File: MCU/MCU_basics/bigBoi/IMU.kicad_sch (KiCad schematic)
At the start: 10 parts, among them U1 BNO086, Y1 32k

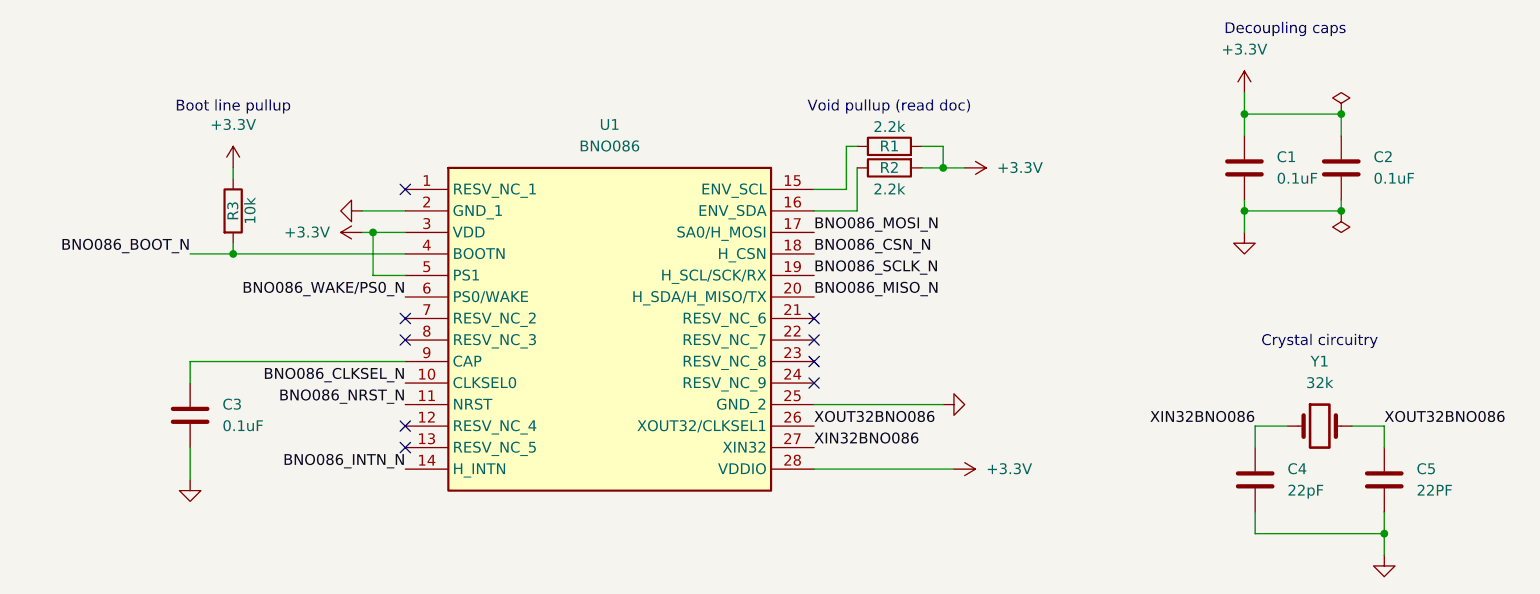
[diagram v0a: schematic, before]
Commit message: schematic connections
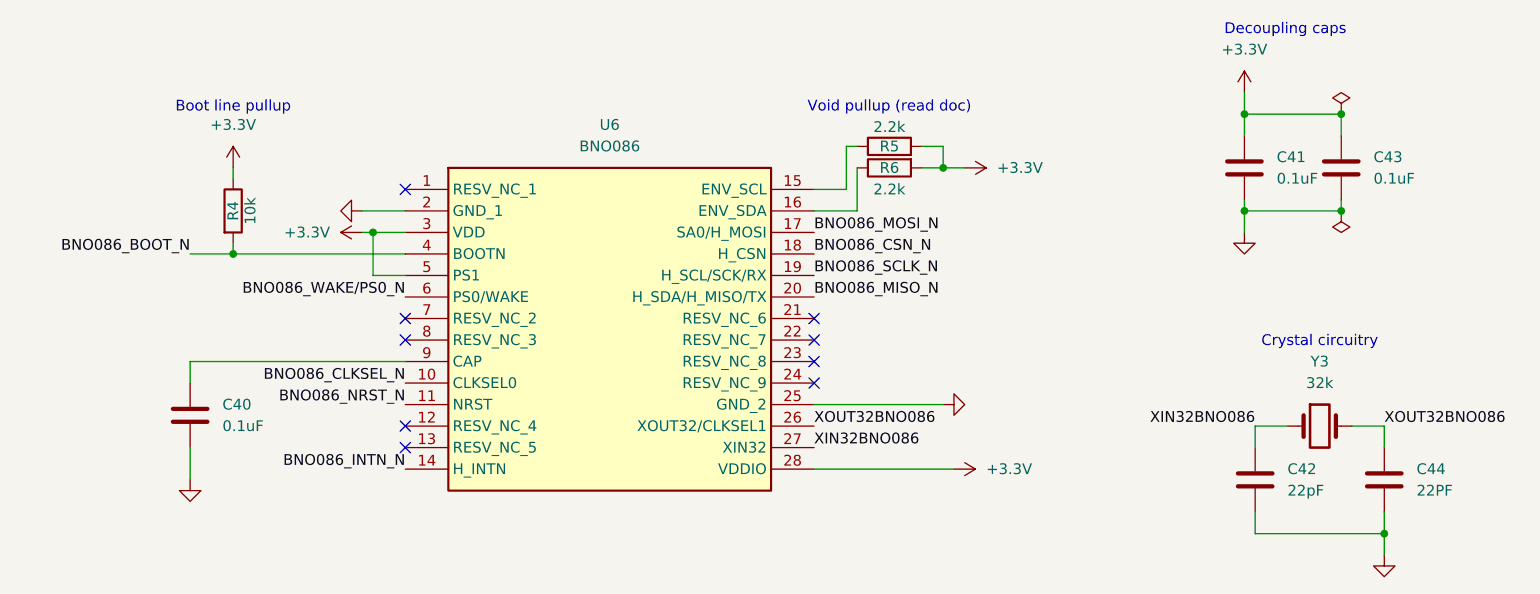
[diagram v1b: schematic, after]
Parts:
- renumbered C3 to C40, C1 to C41, C4 to C42, C2 to C43, C5 to C44, R3 to R4, R1 to R5, R2 to R6, U1 to U6, Y1 to Y3
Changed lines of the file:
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@@
 		(dnp no)
 		(fields_autoplaced yes)
-		(property "Reference" "#PWR046"
+		(property "Reference" "#PWR063"
 			(at 176.53 66.04 0)
 			(hide yes)
@@
 			(project "bigBoi"
 				(path "/0a118c22-2522-42a6-b7a6-70c79326ece4/c267ab07-0814-4d37-8bca-35bdb5036057"
-					(reference "#PWR046")
+					(reference "#PWR063")
 					(unit 1)
 				)
@@
 		(dnp no)
 		(fields_autoplaced yes)
-		(property "Reference" "#PWR040"
+		(property "Reference" "#PWR057"
 			(at 88.9 109.22 0)
 			(hide yes)
@@
 			(project "bigBoi"
 				(path "/0a118c22-2522-42a6-b7a6-70c79326ece4/c267ab07-0814-4d37-8bca-35bdb5036057"
-					(reference "#PWR040")
+					(reference "#PWR057")
 					(unit 1)
 				)
@@
 		(dnp no)
 		(fields_autoplaced yes)
-		(property "Reference" "Y1"
+		(property "Reference" "Y3"
 			(at 222.25 88.9 0)
 			(show_name no)
@@
 			(project "bigBoi"
 				(path "/0a118c22-2522-42a6-b7a6-70c79326ece4/c267ab07-0814-4d37-8bca-35bdb5036057"
-					(reference "Y1")
+					(reference "Y3")
 					(unit 1)
 				)
@@
 		(dnp no)
 		(fields_autoplaced yes)
-		(property "Reference" "C2"
+		(property "Reference" "C43"
 			(at 228.6 64.7699 0)
 			(show_name no)
@@
 			(project "bigBoi"
 				(path "/0a118c22-2522-42a6-b7a6-70c79326ece4/c267ab07-0814-4d37-8bca-35bdb5036057"
-					(reference "C2")
+					(reference "C43")
 					(unit 1)
 				)
@@
 		(in_pos_files yes)
 		(dnp no)
-		(property "Reference" "R2"
+		(property "Reference" "R6"
 			(at 171.45 66.04 90)
 			(show_name no)
@@
 			(project "bigBoi"
 				(path "/0a118c22-2522-42a6-b7a6-70c79326ece4/c267ab07-0814-4d37-8bca-35bdb5036057"
-					(reference "R2")
+					(reference "R6")
 					(unit 1)
 				)
@@
 		(dnp no)
 		(fields_autoplaced yes)
-		(property "Reference" "#PWR047"
+		(property "Reference" "#PWR064"
 			(at 213.36 60.96 0)
 			(hide yes)
@@
 			(project "bigBoi"
 				(path "/0a118c22-2522-42a6-b7a6-70c79326ece4/c267ab07-0814-4d37-8bca-35bdb5036057"
-					(reference "#PWR047")
+					(reference "#PWR064")
 					(unit 1)
 				)
@@
 		(dnp no)
 		(fields_autoplaced yes)
-		(property "Reference" "#PWR049"
+		(property "Reference" "#PWR066"
 			(at 229.87 118.11 0)
 			(hide yes)
@@
 			(project "bigBoi"
 				(path "/0a118c22-2522-42a6-b7a6-70c79326ece4/c267ab07-0814-4d37-8bca-35bdb5036057"
-					(reference "#PWR049")
+					(reference "#PWR066")
 					(unit 1)
 				)
@@
 		(dnp no)
 		(fields_autoplaced yes)
-		(property "Reference" "C3"
+		(property "Reference" "C40"
 			(at 92.71 93.9799 0)
 			(show_name no)
@@
 			(project "bigBoi"
 				(path "/0a118c22-2522-42a6-b7a6-70c79326ece4/c267ab07-0814-4d37-8bca-35bdb5036057"
-					(reference "C3")
+					(reference "C40")
 					(unit 1)
 				)
@@
 		(dnp no)
 		(fields_autoplaced yes)
-		(property "Reference" "U1"
+		(property "Reference" "U6"
 			(at 138.43 60.96 0)
 			(show_name no)
@@
 			(project "bigBoi"
 				(path "/0a118c22-2522-42a6-b7a6-70c79326ece4/c267ab07-0814-4d37-8bca-35bdb5036057"
-					(reference "U1")
+					(reference "U6")
 					(unit 1)
 				)
@@
 		(dnp no)
 		(fields_autoplaced yes)
-		(property "Reference" "#FLG02"
+		(property "Reference" "#FLG03"
 			(at 224.79 57.785 0)
 			(hide yes)
@@
 			(project "bigBoi"
 				(path "/0a118c22-2522-42a6-b7a6-70c79326ece4/c267ab07-0814-4d37-8bca-35bdb5036057"
-					(reference "#FLG02")
+					(reference "#FLG03")
 					(unit 1)
 				)
@@
 		(dnp no)
 		(fields_autoplaced yes)
-		(property "Reference" "C5"
+		(property "Reference" "C44"
 			(at 233.68 101.5999 0)
 			(show_name no)
@@
 			(project "bigBoi"
 				(path "/0a118c22-2522-42a6-b7a6-70c79326ece4/c267ab07-0814-4d37-8bca-35bdb5036057"
-					(reference "C5")
+					(reference "C44")
 					(unit 1)
 				)
@@
 		(dnp no)
 		(fields_autoplaced yes)
-		(property "Reference" "#PWR045"
+		(property "Reference" "#PWR062"
 			(at 175.26 101.6 0)
 			(hide yes)
@@
 			(project "bigBoi"
 				(path "/0a118c22-2522-42a6-b7a6-70c79326ece4/c267ab07-0814-4d37-8bca-35bdb5036057"
-					(reference "#PWR045")
+					(reference "#PWR062")
 					(unit 1)
 				)
@@
 		(dnp no)
 		(fields_autoplaced yes)
-		(property "Reference" "C1"
+		(property "Reference" "C41"
 			(at 217.17 64.7699 0)
 			(show_name no)
@@
 			(project "bigBoi"
 				(path "/0a118c22-2522-42a6-b7a6-70c79326ece4/c267ab07-0814-4d37-8bca-35bdb5036057"
-					(reference "C1")
+					(reference "C41")
 					(unit 1)
 				)
@@
 		(in_pos_files yes)
 		(dnp no)
-		(property "Reference" "R3"
+		(property "Reference" "R4"
 			(at 93.98 71.12 90)
 			(show_name no)
@@
 			(project "bigBoi"
 				(path "/0a118c22-2522-42a6-b7a6-70c79326ece4/c267ab07-0814-4d37-8bca-35bdb5036057"
-					(reference "R3")
+					(reference "R4")
 					(unit 1)
 				)
@@
 		(dnp no)
 		(fields_autoplaced yes)
-		(property "Reference" "#FLG02"
+		(property "Reference" "#FLG04"
 			(at 224.79 73.025 0)
 			(hide yes)
@@
 			(project "bigBoi"
 				(path "/0a118c22-2522-42a6-b7a6-70c79326ece4/c267ab07-0814-4d37-8bca-35bdb5036057"
-					(reference "#FLG02")
+					(reference "#FLG04")
 					(unit 1)
 				)
@@
 		(dnp no)
 		(fields_autoplaced yes)
-		(property "Reference" "#PWR043"
+		(property "Reference" "#PWR060"
 			(at 113.03 73.66 0)
 			(hide yes)
@@
 			(project "bigBoi"
 				(path "/0a118c22-2522-42a6-b7a6-70c79326ece4/c267ab07-0814-4d37-8bca-35bdb5036057"
-					(reference "#PWR043")
+					(reference "#PWR060")
 					(unit 1)
 				)
@@
 		(dnp no)
 		(fields_autoplaced yes)
-		(property "Reference" "#PWR041"
+		(property "Reference" "#PWR058"
 			(at 93.98 69.85 0)
 			(hide yes)
@@
 			(project "bigBoi"
 				(path "/0a118c22-2522-42a6-b7a6-70c79326ece4/c267ab07-0814-4d37-8bca-35bdb5036057"
-					(reference "#PWR041")
+					(reference "#PWR058")
 					(unit 1)
 				)
@@
 		(dnp no)
 		(fields_autoplaced yes)
-		(property "Reference" "C4"
+		(property "Reference" "C42"
 			(at 218.44 101.5999 0)
 			(show_name no)
@@
 			(project "bigBoi"
 				(path "/0a118c22-2522-42a6-b7a6-70c79326ece4/c267ab07-0814-4d37-8bca-35bdb5036057"
-					(reference "C4")
+					(reference "C42")
 					(unit 1)
 				)
@@
 		(dnp no)
 		(fields_autoplaced yes)
-		(property "Reference" "#PWR044"
+		(property "Reference" "#PWR061"
 			(at 184.15 93.98 0)
 			(hide yes)
@@
 			(project "bigBoi"
 				(path "/0a118c22-2522-42a6-b7a6-70c79326ece4/c267ab07-0814-4d37-8bca-35bdb5036057"
-					(reference "#PWR044")
+					(reference "#PWR061")
 					(unit 1)
 				)
@@
 		(dnp no)
 		(fields_autoplaced yes)
-		(property "Reference" "#PWR042"
+		(property "Reference" "#PWR059"
 			(at 102.87 71.12 0)
 			(hide yes)
@@
 			(project "bigBoi"
 				(path "/0a118c22-2522-42a6-b7a6-70c79326ece4/c267ab07-0814-4d37-8bca-35bdb5036057"
-					(reference "#PWR042")
+					(reference "#PWR059")
 					(unit 1)
 				)
@@
 		(dnp no)
 		(fields_autoplaced yes)
-		(property "Reference" "#PWR048"
+		(property "Reference" "#PWR065"
 			(at 213.36 80.01 0)
 			(hide yes)
@@
 			(project "bigBoi"
 				(path "/0a118c22-2522-42a6-b7a6-70c79326ece4/c267ab07-0814-4d37-8bca-35bdb5036057"
-					(reference "#PWR048")
+					(reference "#PWR065")
 					(unit 1)
 				)
@@
 		(in_pos_files yes)
 		(dnp no)
-		(property "Reference" "R1"
+		(property "Reference" "R5"
 			(at 171.45 63.5 90)
 			(show_name no)
@@
 			(project "bigBoi"
 				(path "/0a118c22-2522-42a6-b7a6-70c79326ece4/c267ab07-0814-4d37-8bca-35bdb5036057"
-					(reference "R1")
-					(unit 1)
-				)
+					(reference "R5")
+					(unit 1)
+				)

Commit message: ERC resolving
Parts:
- C40, C41, C42, C43, C44: footprint (none) -> Capacitor_SMD:C_0402_1005Metric
- R4, R5, R6: footprint (none) -> Resistor_SMD:R_0402_1005Metric
- U6: footprint BNO086 -> Nebula-footprints:BNO086
- Y3: value 32k -> 32kHz; footprint (none) -> Crystal:Crystal_SMD_3215-2Pin_3.2x1.5mm

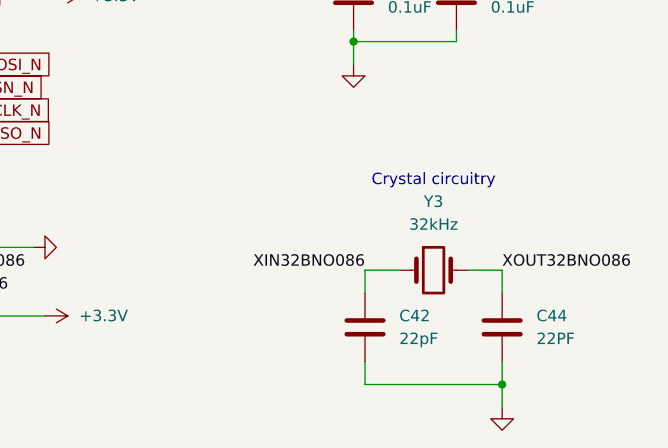
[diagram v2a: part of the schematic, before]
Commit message: Store deler av VBUS og USB
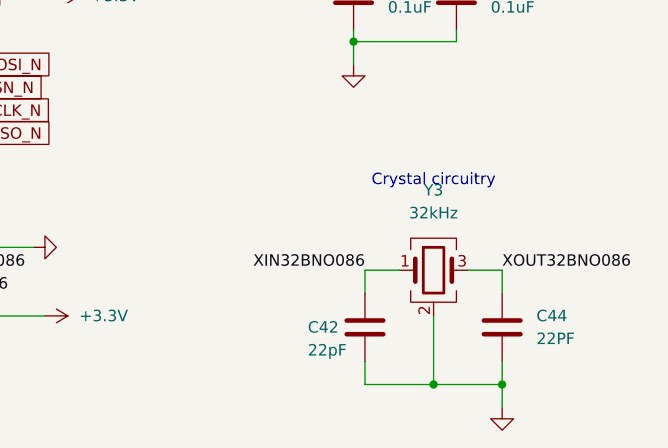
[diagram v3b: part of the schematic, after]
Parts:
- removed Y3: 32kHz, Crystal:Crystal_SMD_3215-2Pin_3.2x1.5mm, symbol Device:Crystal
- added Y3: 32kHz, Crystal:Crystal_SMD_3225-4Pin_3.2x2.5mm_HandSoldering, symbol Device:Crystal_GND24
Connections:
- net GND: now also Y3.2 (G), Y3.4 (G)
- net XIN32BNO086: now also Y3.1
- net XOUT32BNO086: now also Y3.3
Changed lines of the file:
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@@
+	)
+	(junction
+		(at 222.25 109.22)
+		(diameter 0)
+		(color 0 0 0 0)
 	)
 	(junction
@@
 	(wire
 		(pts
+			(xy 222.25 101.6) (xy 222.25 109.22)
+		)
+		(stroke
+			(width 0)
+			(type default)
+		)
+	)
+	(wire
+		(pts
 			(xy 224.79 71.12) (xy 213.36 71.12)
 		)
@@
 	(wire
 		(pts
+			(xy 222.25 109.22) (xy 229.87 109.22)
+		)
+		(stroke
+			(width 0)
+			(type default)
+		)
+	)
+	(wire
+		(pts
 			(xy 166.37 63.5) (xy 166.37 68.58)
 		)
@@
 	(wire
 		(pts
-			(xy 214.63 109.22) (xy 229.87 109.22)
+			(xy 214.63 109.22) (xy 222.25 109.22)
 		)
 		(stroke
@@
 				(path "/0a118c22-2522-42a6-b7a6-70c79326ece4/c267ab07-0814-4d37-8bca-35bdb5036057"
 					(reference "#PWR057")
-					(unit 1)
-				)
-			)
-		)
-	)
-	(symbol
-		(lib_id "Device:Crystal")
-		(at 222.25 96.52 0)
-		(unit 1)
-		(body_style 1)
-		(exclude_from_sim no)
-		(in_bom yes)
-		(on_board yes)
-		(in_pos_files yes)
-		(dnp no)
-		(fields_autoplaced yes)
-		(property "Reference" "Y3"
-			(at 222.25 88.9 0)
-			(show_name no)
-			(do_not_autoplace no)
-			(effects
-				(font
-					(size 1.27 1.27)
-				)
-			)
-		)
-		(property "Value" "32kHz"
-			(at 222.25 91.44 0)
-			(show_name no)
-			(do_not_autoplace no)
-			(effects
-				(font
-					(size 1.27 1.27)
-				)
-			)
-		)
-		(property "Footprint" "Crystal:Crystal_SMD_3215-2Pin_3.2x1.5mm"
-			(at 222.25 96.52 0)
-			(hide yes)
-			(show_name no)
-			(do_not_autoplace no)
-			(effects
-				(font
-					(size 1.27 1.27)
-				)
-			)
-		)
-		(property "Datasheet" ""
-			(at 222.25 96.52 0)
-			(hide yes)
-			(show_name no)
-			(do_not_autoplace no)
-			(effects
-				(font
-					(size 1.27 1.27)
-				)
-			)
-		)
-		(property "Description" "Two pin crystal"
-			(at 222.25 96.52 0)
-			(hide yes)
-			(show_name no)
-			(do_not_autoplace no)
-			(effects
-				(font
-					(size 1.27 1.27)
-				)
-			)
-		)
-		(pin "1"
-		)
-		(pin "2"
-		)
-		(instances
-			(project "bigBoi"
-				(path "/0a118c22-2522-42a6-b7a6-70c79326ece4/c267ab07-0814-4d37-8bca-35bdb5036057"
-					(reference "Y3")
 					(unit 1)
 				)
@@
 	)
 	(symbol
+		(lib_id "Device:Crystal_GND24")
+		(at 222.25 96.52 0)
+		(unit 1)
+		(body_style 1)
+		(exclude_from_sim no)
+		(in_bom yes)
+		(on_board yes)
+		(in_pos_files yes)
+		(dnp no)
+		(fields_autoplaced yes)
+		(property "Reference" "Y3"
+			(at 222.25 87.63 0)
+			(show_name no)
+			(do_not_autoplace no)
+			(effects
+				(font
+					(size 1.27 1.27)
+				)
+			)
+		)
+		(property "Value" "32kHz"
+			(at 222.25 90.17 0)
+			(show_name no)
+			(do_not_autoplace no)
+			(effects
+				(font
+					(size 1.27 1.27)
+				)
+			)
+		)
+		(property "Footprint" "Crystal:Crystal_SMD_3225-4Pin_3.2x2.5mm_HandSoldering"
+			(at 222.25 96.52 0)
+			(hide yes)
+			(show_name no)
+			(do_not_autoplace no)
+			(effects
+				(font
+					(size 1.27 1.27)
+				)
+			)
+		)
+		(property "Datasheet" ""
+			(at 222.25 96.52 0)
+			(hide yes)
+			(show_name no)
+			(do_not_autoplace no)
+			(effects
+				(font
+					(size 1.27 1.27)
+				)
+			)
+		)
+		(property "Description" "Four pin crystal, GND on pins 2 and 4"
+			(at 222.25 96.52 0)
+			(hide yes)
+			(show_name no)
+			(do_not_autoplace no)
+			(effects
+				(font
+					(size 1.27 1.27)
+				)
+			)
+		)
+		(property private "KLC_S3.3" "The rectangle is not a symbol body but a graphical element"
+			(at 222.25 109.22 0)
+			(hide yes)
+			(show_name yes)
+			(do_not_autoplace no)
+			(effects
+				(font
+					(size 1.27 1.27)
+				)
+			)
+		)
+		(property private "KLC_S4.1" "Some pins are on 50mil grid to make the symbol small"
+			(at 222.25 111.76 0)
+			(hide yes)
+			(show_name yes)
+			(do_not_autoplace no)
+			(effects
+				(font
+					(size 1.27 1.27)
+				)
+			)
+		)
+		(pin "1"
+		)
+		(pin "3"
+		)
+		(pin "2"
+		)
+		(pin "4"
+		)
+		(instances
+			(project "bigBoi"
+				(path "/0a118c22-2522-42a6-b7a6-70c79326ece4/c267ab07-0814-4d37-8bca-35bdb5036057"
+					(reference "Y3")
+					(unit 1)
+				)
+			)
+		)
+	)
+	(symbol
 		(lib_id "Device:C")
 		(at 229.87 102.87 0)
@@
 		(in_pos_files yes)
 		(dnp no)
-		(fields_autoplaced yes)
 		(property "Reference" "C42"
-			(at 218.44 101.5999 0)
+			(at 208.28 102.87 0)
 			(show_name no)
 			(do_not_autoplace no)
@@
 		)
 		(property "Value" "22pF"
-			(at 218.44 104.1399 0)
-			(show_name no)
-			(do_not_autoplace no)
+			(at 208.28 105.41 0)
+			(show_name no)
+			(do_not_autoplace no)

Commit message: SX1276 layout
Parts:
- Y3: footprint Crystal:Crystal_SMD_3225-4Pin_3.2x2.5mm_HandSoldering -> Crystal:Crystal_SMD_3225-4Pin_3.2x2.5mm
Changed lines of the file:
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@@
 			)
 		)
-		(property "Footprint" "Crystal:Crystal_SMD_3225-4Pin_3.2x2.5mm_HandSoldering"
+		(property "Footprint" "Crystal:Crystal_SMD_3225-4Pin_3.2x2.5mm"
 			(at 222.25 96.52 0)
 			(hide yes)

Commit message: routing complete
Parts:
- added C60: 1uF, Capacitor_SMD:C_0402_1005Metric, symbol Device:C
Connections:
- net +3.3V: now also C60.1
- net GND: now also C60.2
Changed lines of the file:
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@@
+	(wire
+		(pts
+			(xy 200.66 69.85) (xy 200.66 71.12)
+		)
+		(stroke
+			(width 0)
+			(type default)
+		)
+	)
 	(wire
 		(pts
@@
 	(wire
 		(pts
+			(xy 200.66 59.69) (xy 213.36 59.69)
+		)
+		(stroke
+			(width 0)
+			(type default)
+		)
+	)
+	(wire
+		(pts
 			(xy 213.36 57.15) (xy 213.36 59.69)
 		)
@@
 	(wire
 		(pts
+			(xy 200.66 71.12) (xy 213.36 71.12)
+		)
+		(stroke
+			(width 0)
+			(type default)
+		)
+	)
+	(wire
+		(pts
 			(xy 222.25 101.6) (xy 222.25 109.22)
 		)
@@
 		(pts
 			(xy 162.56 101.6) (xy 179.07 101.6)
+		)
+		(stroke
+			(width 0)
+			(type default)
+		)
+	)
+	(wire
+		(pts
+			(xy 200.66 62.23) (xy 200.66 59.69)
 		)
 		(stroke
@@
 					(unit 1)
 				)
+			)
+		)
+	)
+	(symbol
+		(lib_id "Device:C")
+		(at 200.66 66.04 0)
+		(unit 1)
+		(body_style 1)
+		(exclude_from_sim no)
+		(in_bom yes)
+		(on_board yes)
+		(in_pos_files yes)
+		(dnp no)
+		(fields_autoplaced yes)
+		(property "Reference" "C60"
+			(at 204.47 64.7699 0)
+			(show_name no)
+			(do_not_autoplace no)
+			(effects
+				(font
+					(size 1.27 1.27)
+				)
+				(justify left)
+			)
+		)
+		(property "Value" "1uF"
+			(at 204.47 67.3099 0)
+			(show_name no)
+			(do_not_autoplace no)
+			(effects
+				(font
+					(size 1.27 1.27)
+				)
+				(justify left)
+			)
+		)
+		(property "Footprint" "Capacitor_SMD:C_0402_1005Metric"
+			(at 201.6252 69.85 0)
+			(hide yes)
+			(show_name no)
+			(do_not_autoplace no)
+			(effects
+				(font
+					(size 1.27 1.27)
+				)
+			)
+		)
+		(property "Datasheet" ""
+			(at 200.66 66.04 0)
+			(hide yes)
+			(show_name no)
+			(do_not_autoplace no)
+			(effects
+				(font
+					(size 1.27 1.27)
+				)
+			)
+		)
+		(property "Description" "Unpolarized capacitor"
+			(at 200.66 66.04 0)
+			(hide yes)
+			(show_name no)
+			(do_not_autoplace no)
+			(effects
+				(font
+					(size 1.27 1.27)
+				)
+			)
+		)
+		(pin "1"
+		)
+		(pin "2"
+		)
+		(instances
+			(project "bigBoi"
+				(path "/0a118c22-2522-42a6-b7a6-70c79326ece4/c267ab07-0814-4d37-8bca-35bdb5036057"
+					(reference "C60")
+					(unit 1)
+				)
